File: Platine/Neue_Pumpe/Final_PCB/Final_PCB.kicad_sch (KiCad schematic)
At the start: 25 parts, among them J1 Conn_01x12, J10 Conn_01x02, J11 Conn_01x05, J12 Conn_01x05, J13 Conn_01x05, J2 Conn_01x10, J3 Conn_01x10, J4 Conn_01x10, J5 Conn_01x10, J6 Conn_01x08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

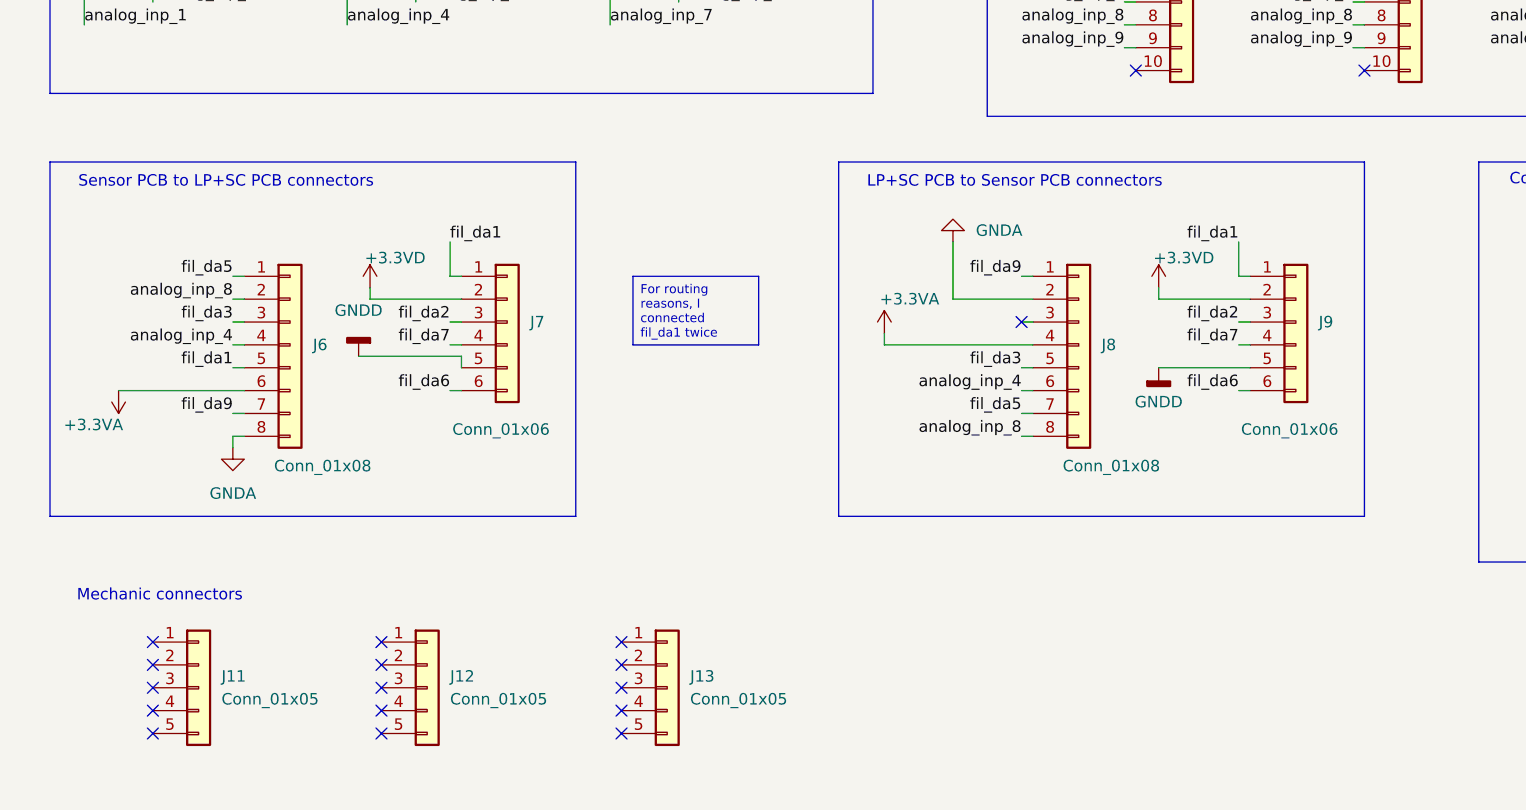
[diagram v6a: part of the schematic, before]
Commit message: Changed connectors according to stock. Added auxiliar projects for printing each PCB, added component list
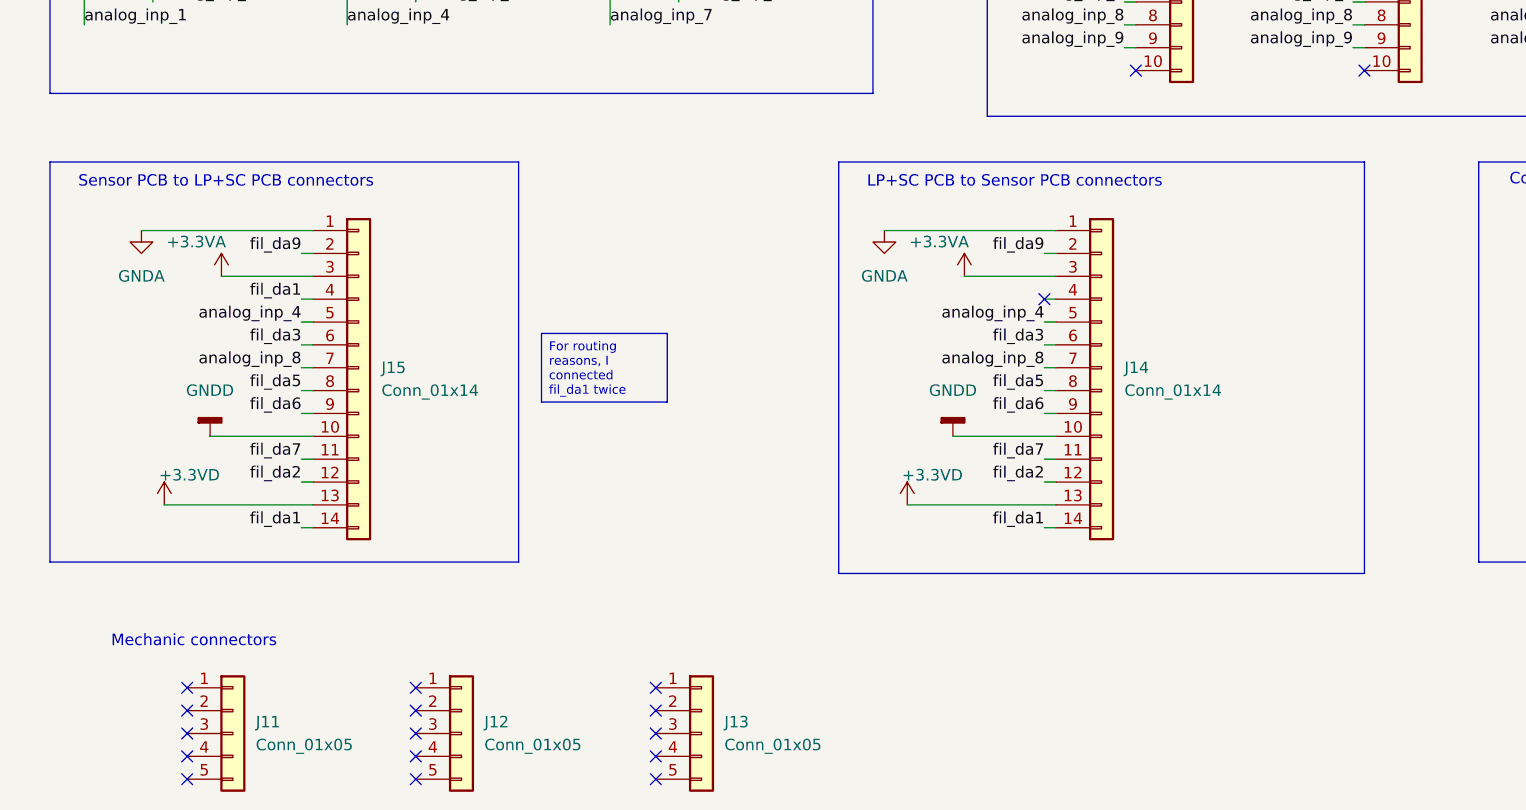
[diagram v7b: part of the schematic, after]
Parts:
- removed J6: Conn_01x08, Connector_PinHeader_1.27mm_modified:PinHeader_2x04_P1.27mm_Vertical_SMD, symbol Connector_Generic:Conn_01x08
- removed J7: Conn_01x06, Connector_PinHeader_1.27mm:PinHeader_2x03_P1.27mm_Vertical_SMD, symbol Connector_Generic:Conn_01x06
- removed J8: Conn_01x08, Connector_PinHeader_1.27mm:PinHeader_2x04_P1.27mm_Horizontal, symbol Connector_Generic:Conn_01x08
- removed J9: Conn_01x06, Connector_PinHeader_1.27mm:PinHeader_2x03_P1.27mm_Horizontal, symbol Connector_Generic:Conn_01x06
- added J14: Conn_01x14, FTS-107-01-L-D-P:SAMTEC_FTS-107-01-L-D, symbol Connector_Generic:Conn_01x14
- added J15: Conn_01x14, FTSH-107-01-L-DV-K:SAMTEC_FTSH-107-01-L-DV-K, symbol Connector_Generic:Conn_01x14
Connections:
- net +3.3VA: now also J14.3 (Pin_3), J15.3 (Pin_3)
- net +3.3VD: now also J14.13 (Pin_13), J15.13 (Pin_13)
- net GNDA: now also J14.1 (Pin_1), J15.1 (Pin_1)
- net GNDD: now also J14.10 (Pin_10), J15.10 (Pin_10)
- net analog_inp_4: now also J14.5 (Pin_5), J15.5 (Pin_5)
- net analog_inp_8: now also J14.7 (Pin_7), J15.7 (Pin_7)
- net fil_da1: now also J14.14 (Pin_14), J15.14 (Pin_14), J15.4 (Pin_4)
- net fil_da2: now also J14.12 (Pin_12), J15.12 (Pin_12)
- net fil_da3: now also J14.6 (Pin_6), J15.6 (Pin_6)
- net fil_da5: now also J14.8 (Pin_8), J15.8 (Pin_8)
- net fil_da6: now also J14.9 (Pin_9), J15.9 (Pin_9)
- net fil_da7: now also J14.11 (Pin_11), J15.11 (Pin_11)
- net fil_da9: now also J14.2 (Pin_2), J15.2 (Pin_2)
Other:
- moved on the sheet: J11, J12, J13
